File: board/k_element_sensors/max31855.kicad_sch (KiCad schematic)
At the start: 4 parts, among them J9 Screw_Terminal_01x02, U7 MAX31855KASA+T

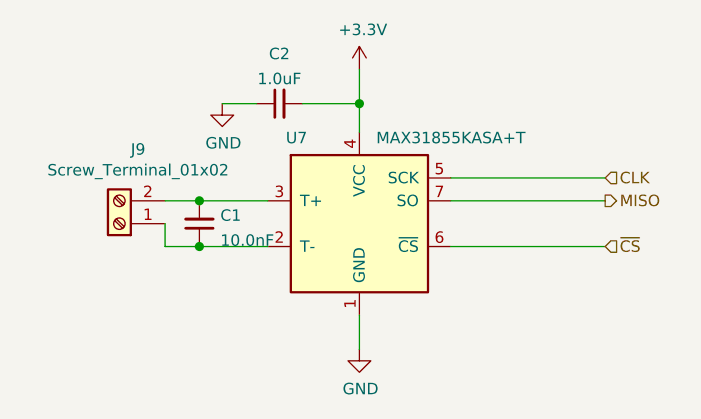
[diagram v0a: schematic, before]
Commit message: Update phase-angle-control-board to handle more current
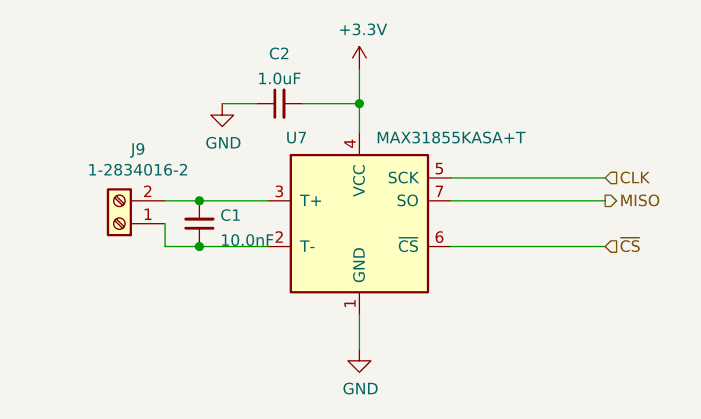
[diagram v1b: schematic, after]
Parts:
- C1: LCSC Part# (none) -> C389113
- C2: LCSC Part# (none) -> C328910
- J9: value Screw_Terminal_01x02 -> 1-2834016-2; LCSC Part# (none) -> C474892
- U7: LCSC Part # C52028 -> (none); LCSC Part# (none) -> C52028
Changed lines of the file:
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@@
+      (effects (font (size 1.27 1.27)) hide)
+    )
+    (property "LCSC Part#" "C389113" (id 4) (at 118.11 91.44 0)
       (effects (font (size 1.27 1.27)) hide)
     )
@@
       (effects (font (size 1.27 1.27)) hide)
     )
+    (property "LCSC Part#" "C328910" (id 4) (at 127 78.105 90)
+      (effects (font (size 1.27 1.27)) hide)
+    )
     (pin "1")
     (pin "2")
@@
     (in_bom yes) (on_board yes)
     (property "Reference" "J9" (id 0) (at 111.3028 83.185 0))
-    (property "Value" "Screw_Terminal_01x02" (id 1) (at 111.3028 85.4964 0))
+    (property "Value" "1-2834016-2 " (id 1) (at 111.3028 85.4964 0))
     (property "Footprint" "pac:con_A123829-ND‎" (id 2) (at 109.22 91.44 0)
       (effects (font (size 1.27 1.27)) hide)
@@
     )
     (property "LCSC Part #" "C474892" (id 4) (at 109.22 91.44 0)
+      (effects (font (size 1.27 1.27)) hide)
+    )
+    (property "LCSC Part#" "C474892" (id 5) (at 109.22 91.44 0)
       (effects (font (size 1.27 1.27)) hide)
     )
@@
       (effects (font (size 1.27 1.27)) hide)
     )
-    (property "LCSC Part #" "C52028" (id 4) (at 135.89 91.44 0)
+    (property "LCSC Part#" "C52028" (id 4) (at 135.89 91.44 0)
       (effects (font (size 1.27 1.27)) hide)
     )

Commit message: Fix LED rotation
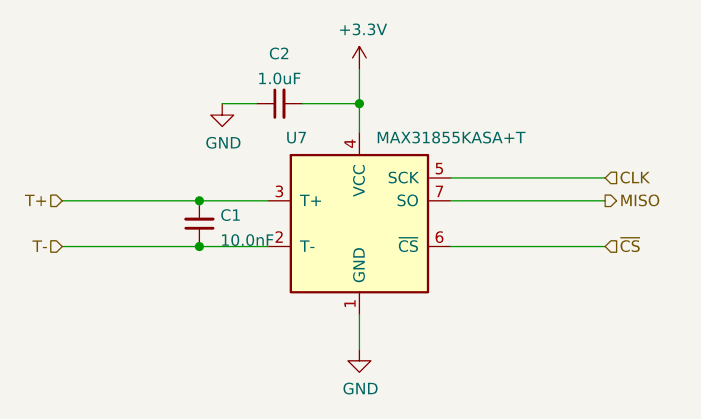
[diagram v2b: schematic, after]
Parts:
- removed J9: 1-2834016-2, pac:con_A123829-ND‎, symbol Connector:Screw_Terminal_01x02
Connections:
- net T-: now reaches C1.1, U7.2 (T-)
- net T+: now reaches C1.2, U7.3 (T+)
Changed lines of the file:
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@@
   (junction (at 118.11 93.98) (diameter 1.016) (color 0 0 0 0))
   (junction (at 135.89 78.105) (diameter 1.016) (color 0 0 0 0))
-  (wire (pts (xy 114.3 88.9) (xy 118.11 88.9))
+  (wire (pts (xy 102.87 88.9) (xy 118.11 88.9))
     (stroke (width 0) (type solid) (color 0 0 0 0))
   )
-  (wire (pts (xy 114.3 91.44) (xy 114.3 93.98))
-    (stroke (width 0) (type solid) (color 0 0 0 0))
-  )
-  (wire (pts (xy 114.3 93.98) (xy 118.11 93.98))
+  (wire (pts (xy 102.87 93.98) (xy 118.11 93.98))
     (stroke (width 0) (type solid) (color 0 0 0 0))
   )
@@
   (wire (pts (xy 163.195 93.98) (xy 146.05 93.98))
     (stroke (width 0) (type solid) (color 0 0 0 0))
+  )
+  (hierarchical_label "T+" (shape input) (at 102.87 88.9 180)
+    (effects (font (size 1.27 1.27)) (justify right))
+  )
+  (hierarchical_label "T-" (shape input) (at 102.87 93.98 180)
+    (effects (font (size 1.27 1.27)) (justify right))
   )
   (hierarchical_label "CLK" (shape input) (at 163.195 86.36 0)
@@
       (effects (font (size 1.27 1.27)) hide)
     )
-    (pin "1")
-    (pin "2")
-  )
-  (symbol (lib_id "Connector:Screw_Terminal_01x02") (at 109.22 91.44 180) (unit 1)
-    (in_bom yes) (on_board yes)
-    (property "Reference" "J9" (id 0) (at 111.3028 83.185 0))
-    (property "Value" "1-2834016-2 " (id 1) (at 111.3028 85.4964 0))
-    (property "Footprint" "pac:con_A123829-ND‎" (id 2) (at 109.22 91.44 0)
-      (effects (font (size 1.27 1.27)) hide)
-    )
-    (property "Datasheet" "~" (id 3) (at 109.22 91.44 0)
-      (effects (font (size 1.27 1.27)) hide)
-    )
-    (property "LCSC Part #" "C474892" (id 4) (at 109.22 91.44 0)
-      (effects (font (size 1.27 1.27)) hide)
-    )
-    (property "LCSC Part#" "C474892" (id 5) (at 109.22 91.44 0)
-      (effects (font (size 1.27 1.27)) hide)
-    )
